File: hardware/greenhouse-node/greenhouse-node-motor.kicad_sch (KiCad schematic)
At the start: 15 parts, among them J7 Conn_01x02_Male, Q2 BC549C, Q3 IRF9530N, Q4 IRF530N, Q6 IRF9530N, Q7 IRF530N, Q8 BC549C

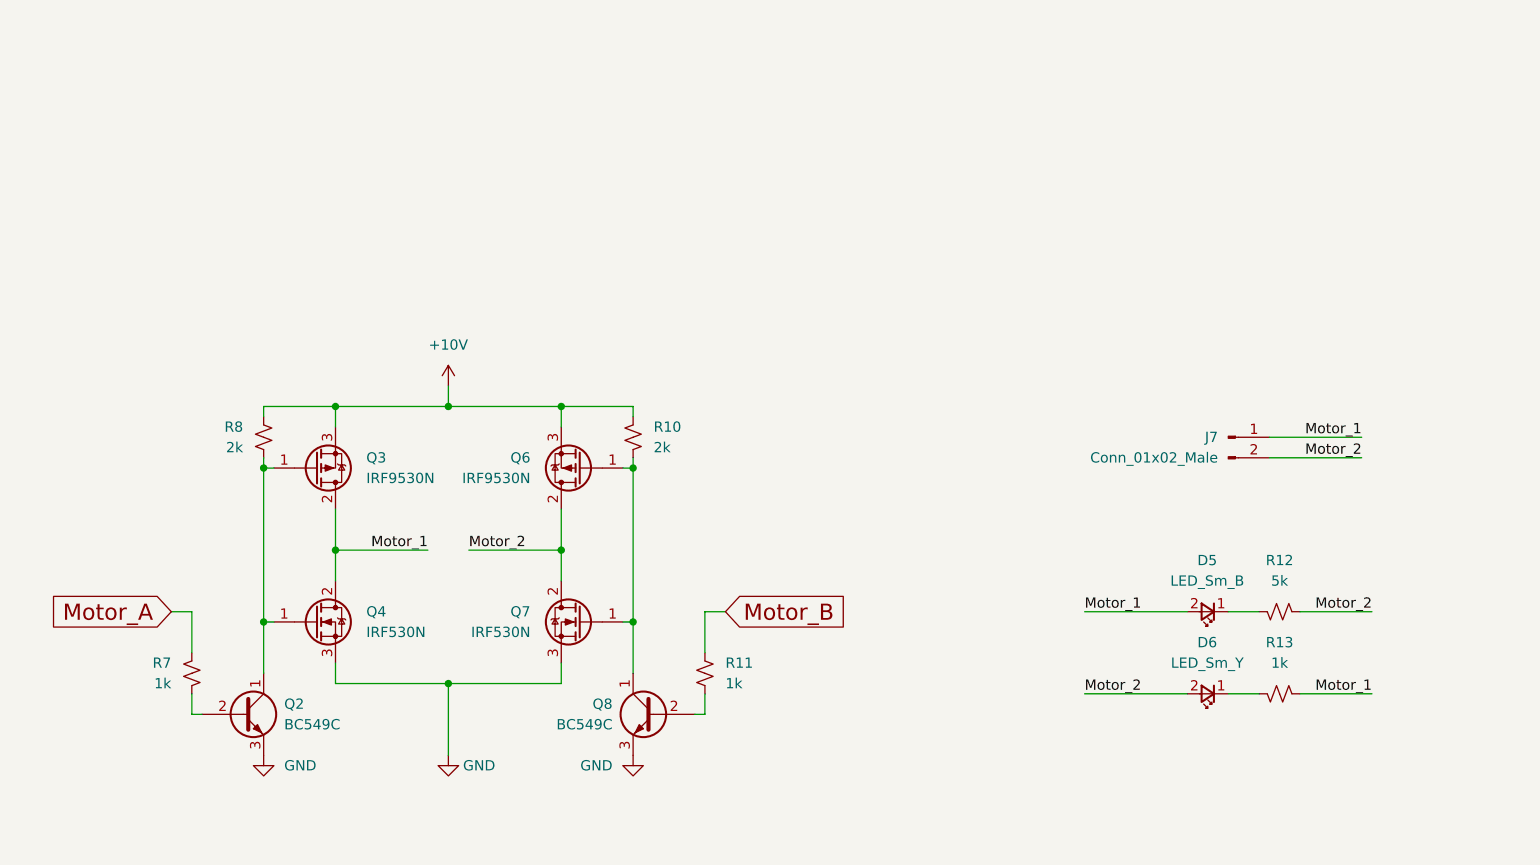
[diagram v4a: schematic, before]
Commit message: Make H-bridge PWM enabled
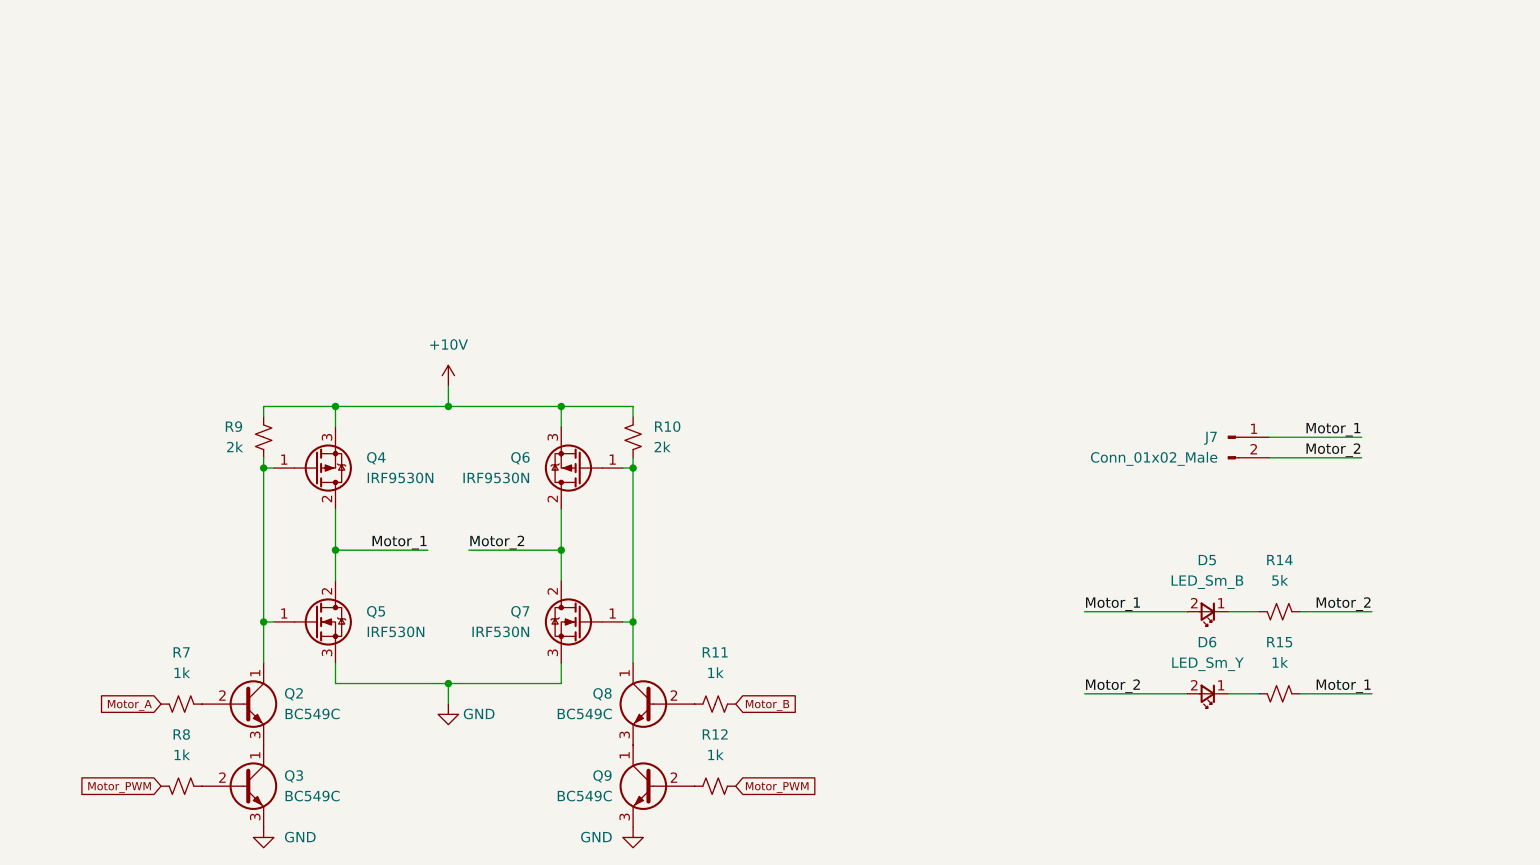
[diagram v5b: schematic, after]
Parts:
- added Q2, Q8: BC549C, Package_TO_SOT_THT:TO-92_Inline, symbol Transistor_BJT:BC549
- added R11, R7: 1k, Resistor_THT:R_Axial_DIN0204_L3.6mm_D1.6mm_P7.62mm_Horizontal, symbol Device:R_Small_US
- renumbered Q2 to Q3, Q3 to Q4, Q4 to Q5, Q8 to Q9, R11 to R12, R12 to R14, R13 to R15, R7 to R8, R8 to R9
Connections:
- net Motor_A: now also R7.2; no longer R8.2
- net Motor_B: now also R11.2; no longer R12.2
- net at Q6.1 (G), Q7.1 (G), R10.1: now also Q8.1 (C); no longer Q9.1 (C)
- net at Q4.1 (G), Q5.1 (G), R9.1: now also Q2.1 (C); no longer Q3.1 (C)
- new net: Q8.3 (E), Q9.1 (C)
- new net: Q2.3 (E), Q3.1 (C)
- new net: Q8.2 (B), R11.1
- new net: Q2.2 (B), R7.1
- new net Motor_PWM: R12.2, R8.2
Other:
- moved on the sheet: Q3, Q9, R12, R8

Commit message: Add pull downs to SR SER+CLK
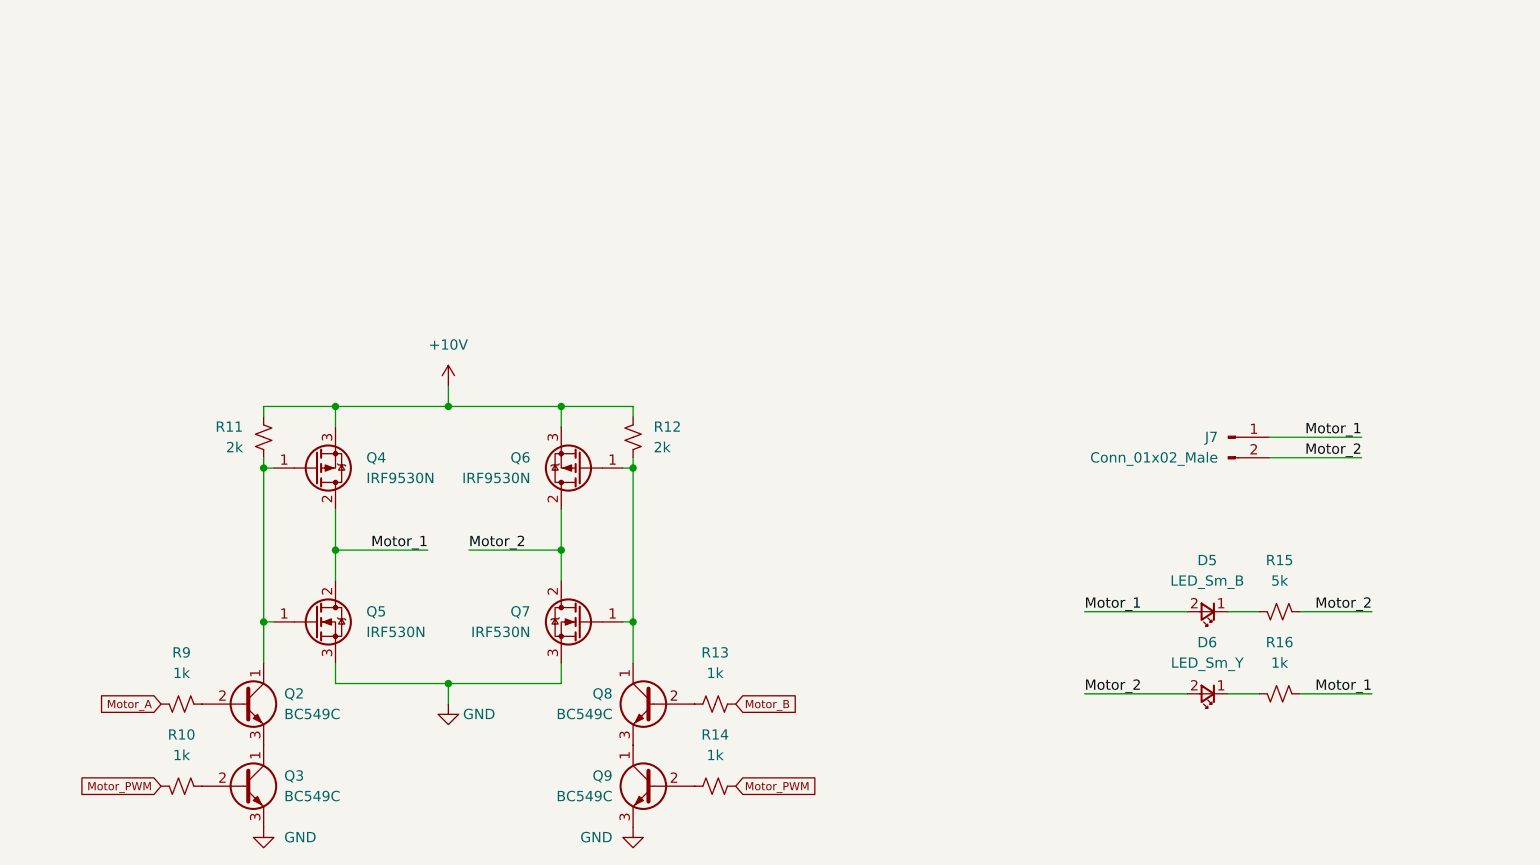
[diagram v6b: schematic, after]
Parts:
- renumbered R8 to R10, R9 to R11, R10 to R12, R11 to R13, R12 to R14, R14 to R15, R15 to R16, R7 to R9
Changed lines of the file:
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@@
   (symbol (lib_id "Device:R_Small_US") (at 69.85 142.24 270) (mirror x) (unit 1)
     (in_bom yes) (on_board yes) (fields_autoplaced)
-    (property "Reference" "R8" (id 0) (at 69.85 135.89 90))
+    (property "Reference" "R10" (id 0) (at 69.85 135.89 90))
     (property "Value" "1k" (id 1) (at 69.85 138.43 90))
     (property "Footprint" "Resistor_THT:R_Axial_DIN0204_L3.6mm_D1.6mm_P7.62mm_Horizontal" (id 2) (at 69.85 142.24 0)
@@
   (symbol (lib_id "power:+10V") (at 102.87 92.71 0) (unit 1)
     (in_bom yes) (on_board yes) (fields_autoplaced)
-    (property "Reference" "#PWR021" (id 0) (at 102.87 96.52 0)
+    (property "Reference" "#PWR022" (id 0) (at 102.87 96.52 0)
       (effects (font (size 1.27 1.27)) hide)
     )
@@
   (symbol (lib_id "Device:R_Small_US") (at 135.89 132.08 90) (unit 1)
     (in_bom yes) (on_board yes) (fields_autoplaced)
-    (property "Reference" "R11" (id 0) (at 135.89 125.73 90))
+    (property "Reference" "R13" (id 0) (at 135.89 125.73 90))
     (property "Value" "1k" (id 1) (at 135.89 128.27 90))
     (property "Footprint" "Resistor_THT:R_Axial_DIN0204_L3.6mm_D1.6mm_P7.62mm_Horizontal" (id 2) (at 135.89 132.08 0)
@@
   (symbol (lib_id "Device:R_Small_US") (at 135.89 142.24 90) (unit 1)
     (in_bom yes) (on_board yes) (fields_autoplaced)
-    (property "Reference" "R12" (id 0) (at 135.89 135.89 90))
+    (property "Reference" "R14" (id 0) (at 135.89 135.89 90))
     (property "Value" "1k" (id 1) (at 135.89 138.43 90))
     (property "Footprint" "Resistor_THT:R_Axial_DIN0204_L3.6mm_D1.6mm_P7.62mm_Horizontal" (id 2) (at 135.89 142.24 0)
@@
   (symbol (lib_id "Device:R_Small_US") (at 69.85 132.08 270) (mirror x) (unit 1)
     (in_bom yes) (on_board yes) (fields_autoplaced)
-    (property "Reference" "R7" (id 0) (at 69.85 125.73 90))
+    (property "Reference" "R9" (id 0) (at 69.85 125.73 90))
     (property "Value" "1k" (id 1) (at 69.85 128.27 90))
     (property "Footprint" "Resistor_THT:R_Axial_DIN0204_L3.6mm_D1.6mm_P7.62mm_Horizontal" (id 2) (at 69.85 132.08 0)
@@
   (symbol (lib_id "Device:R_Small_US") (at 80.01 99.06 180) (unit 1)
     (in_bom yes) (on_board yes) (fields_autoplaced)
-    (property "Reference" "R9" (id 0) (at 77.47 97.7899 0)
+    (property "Reference" "R11" (id 0) (at 77.47 97.7899 0)
       (effects (font (size 1.27 1.27)) (justify left))
     )
@@
   (symbol (lib_id "Device:R_Small_US") (at 125.73 99.06 0) (mirror x) (unit 1)
     (in_bom yes) (on_board yes)
-    (property "Reference" "R10" (id 0) (at 128.27 97.7899 0)
+    (property "Reference" "R12" (id 0) (at 128.27 97.7899 0)
       (effects (font (size 1.27 1.27)) (justify left))
     )
@@
   (symbol (lib_id "Device:R_Small_US") (at 205.74 130.81 270) (mirror x) (unit 1)
     (in_bom yes) (on_board yes) (fields_autoplaced)
-    (property "Reference" "R15" (id 0) (at 205.74 124.46 90))
+    (property "Reference" "R16" (id 0) (at 205.74 124.46 90))
     (property "Value" "1k" (id 1) (at 205.74 127 90))
     (property "Footprint" "Resistor_THT:R_Axial_DIN0204_L3.6mm_D1.6mm_P7.62mm_Horizontal" (id 2) (at 205.74 130.81 0)
@@
   (symbol (lib_id "Device:R_Small_US") (at 205.74 120.65 270) (mirror x) (unit 1)
     (in_bom yes) (on_board yes) (fields_autoplaced)
-    (property "Reference" "R14" (id 0) (at 205.74 114.3 90))
+    (property "Reference" "R15" (id 0) (at 205.74 114.3 90))
     (property "Value" "5k" (id 1) (at 205.74 116.84 90))
     (property "Footprint" "Resistor_THT:R_Axial_DIN0204_L3.6mm_D1.6mm_P7.62mm_Horizontal" (id 2) (at 205.74 120.65 0)
@@
   (symbol (lib_id "power:GND") (at 102.87 132.08 0) (unit 1)
     (in_bom yes) (on_board yes)
-    (property "Reference" "#PWR022" (id 0) (at 102.87 138.43 0)
+    (property "Reference" "#PWR023" (id 0) (at 102.87 138.43 0)
       (effects (font (size 1.27 1.27)) hide)
     )
@@
   (symbol (lib_id "power:GND") (at 80.01 147.32 0) (unit 1)
     (in_bom yes) (on_board yes) (fields_autoplaced)
-    (property "Reference" "#PWR020" (id 0) (at 80.01 153.67 0)
+    (property "Reference" "#PWR021" (id 0) (at 80.01 153.67 0)
       (effects (font (size 1.27 1.27)) hide)
     )
@@
   (symbol (lib_id "power:GND") (at 125.73 147.32 0) (mirror y) (unit 1)
     (in_bom yes) (on_board yes) (fields_autoplaced)
-    (property "Reference" "#PWR023" (id 0) (at 125.73 153.67 0)
-      (effects (font (size 1.27 1.27)) hide)
-    )
+    (property "Reference" "#PWR024" (id 0) (at 125.73 153.67 0)
+      (effects (font (size 1.27 1.27)) hide)
+    )

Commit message: Micro programming connector
Also:
- Connect SRCLR to +5V
- Move 10V pull-up away from micro
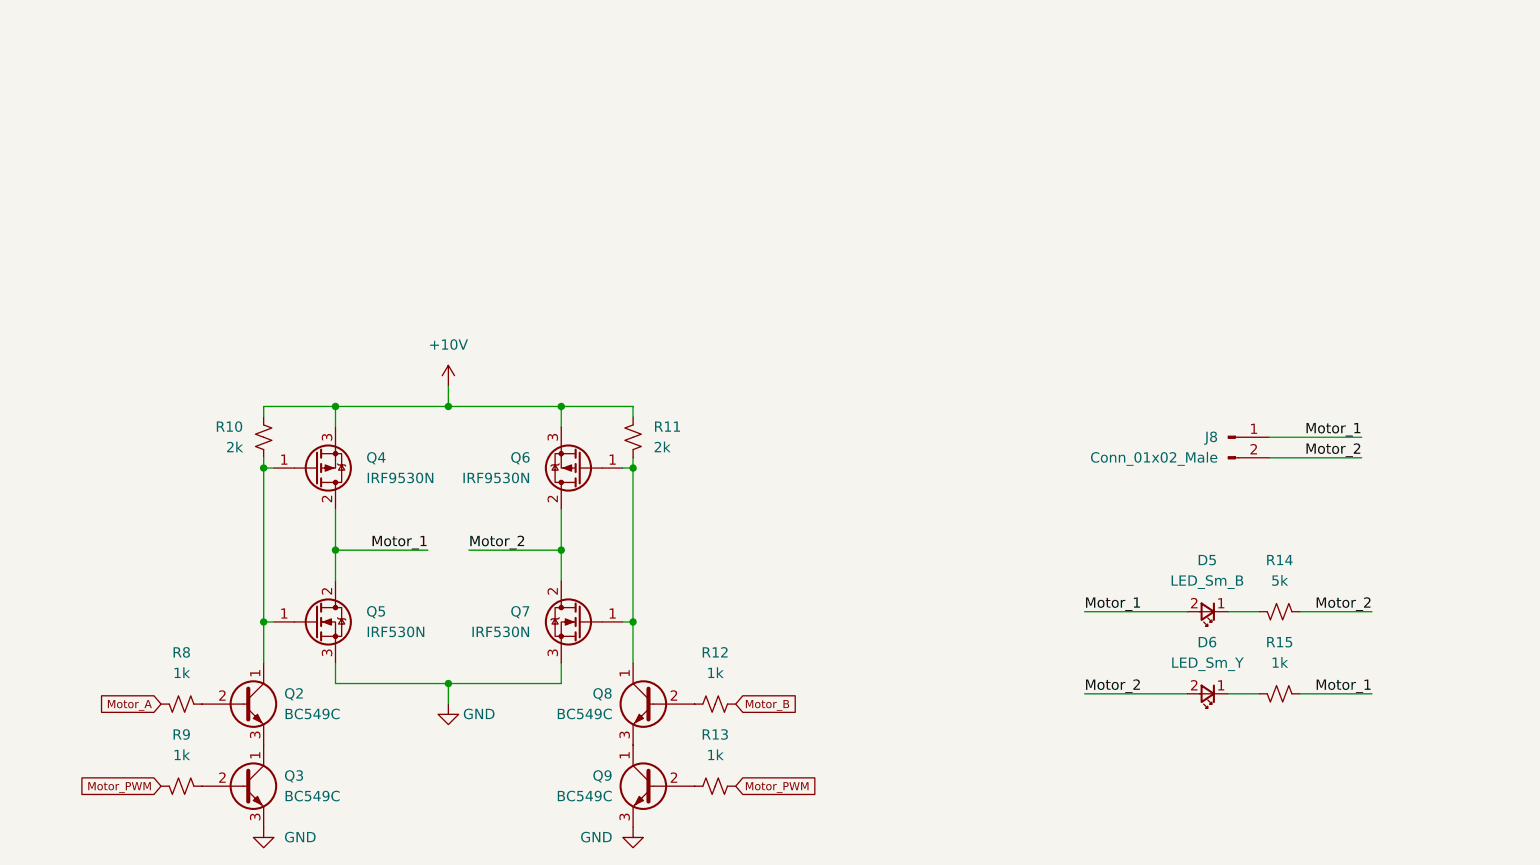
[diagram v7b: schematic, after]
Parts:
- renumbered J7 to J8, R11 to R10, R12 to R11, R13 to R12, R14 to R13, R15 to R14, R16 to R15, R9 to R8, R10 to R9
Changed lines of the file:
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@@
   (symbol (lib_id "Device:R_Small_US") (at 69.85 142.24 270) (mirror x) (unit 1)
     (in_bom yes) (on_board yes) (fields_autoplaced)
-    (property "Reference" "R10" (id 0) (at 69.85 135.89 90))
+    (property "Reference" "R9" (id 0) (at 69.85 135.89 90))
     (property "Value" "1k" (id 1) (at 69.85 138.43 90))
     (property "Footprint" "Resistor_THT:R_Axial_DIN0204_L3.6mm_D1.6mm_P7.62mm_Horizontal" (id 2) (at 69.85 142.24 0)
@@
   (symbol (lib_id "power:+10V") (at 102.87 92.71 0) (unit 1)
     (in_bom yes) (on_board yes) (fields_autoplaced)
-    (property "Reference" "#PWR022" (id 0) (at 102.87 96.52 0)
+    (property "Reference" "#PWR023" (id 0) (at 102.87 96.52 0)
       (effects (font (size 1.27 1.27)) hide)
     )
@@
   (symbol (lib_id "Device:R_Small_US") (at 135.89 132.08 90) (unit 1)
     (in_bom yes) (on_board yes) (fields_autoplaced)
-    (property "Reference" "R13" (id 0) (at 135.89 125.73 90))
+    (property "Reference" "R12" (id 0) (at 135.89 125.73 90))
     (property "Value" "1k" (id 1) (at 135.89 128.27 90))
     (property "Footprint" "Resistor_THT:R_Axial_DIN0204_L3.6mm_D1.6mm_P7.62mm_Horizontal" (id 2) (at 135.89 132.08 0)
@@
   (symbol (lib_id "Connector:Conn_01x02_Male") (at 199.39 99.06 0) (unit 1)
     (in_bom yes) (on_board yes) (fields_autoplaced)
-    (property "Reference" "J7" (id 0) (at 198.12 99.0599 0)
+    (property "Reference" "J8" (id 0) (at 198.12 99.0599 0)
       (effects (font (size 1.27 1.27)) (justify right))
     )
@@
   (symbol (lib_id "Device:R_Small_US") (at 135.89 142.24 90) (unit 1)
     (in_bom yes) (on_board yes) (fields_autoplaced)
-    (property "Reference" "R14" (id 0) (at 135.89 135.89 90))
+    (property "Reference" "R13" (id 0) (at 135.89 135.89 90))
     (property "Value" "1k" (id 1) (at 135.89 138.43 90))
     (property "Footprint" "Resistor_THT:R_Axial_DIN0204_L3.6mm_D1.6mm_P7.62mm_Horizontal" (id 2) (at 135.89 142.24 0)
@@
   (symbol (lib_id "Device:R_Small_US") (at 69.85 132.08 270) (mirror x) (unit 1)
     (in_bom yes) (on_board yes) (fields_autoplaced)
-    (property "Reference" "R9" (id 0) (at 69.85 125.73 90))
+    (property "Reference" "R8" (id 0) (at 69.85 125.73 90))
     (property "Value" "1k" (id 1) (at 69.85 128.27 90))
     (property "Footprint" "Resistor_THT:R_Axial_DIN0204_L3.6mm_D1.6mm_P7.62mm_Horizontal" (id 2) (at 69.85 132.08 0)
@@
   (symbol (lib_id "Device:R_Small_US") (at 80.01 99.06 180) (unit 1)
     (in_bom yes) (on_board yes) (fields_autoplaced)
-    (property "Reference" "R11" (id 0) (at 77.47 97.7899 0)
+    (property "Reference" "R10" (id 0) (at 77.47 97.7899 0)
       (effects (font (size 1.27 1.27)) (justify left))
     )
@@
   (symbol (lib_id "Device:R_Small_US") (at 125.73 99.06 0) (mirror x) (unit 1)
     (in_bom yes) (on_board yes)
-    (property "Reference" "R12" (id 0) (at 128.27 97.7899 0)
+    (property "Reference" "R11" (id 0) (at 128.27 97.7899 0)
       (effects (font (size 1.27 1.27)) (justify left))
     )
@@
   (symbol (lib_id "Device:R_Small_US") (at 205.74 130.81 270) (mirror x) (unit 1)
     (in_bom yes) (on_board yes) (fields_autoplaced)
-    (property "Reference" "R16" (id 0) (at 205.74 124.46 90))
+    (property "Reference" "R15" (id 0) (at 205.74 124.46 90))
     (property "Value" "1k" (id 1) (at 205.74 127 90))
     (property "Footprint" "Resistor_THT:R_Axial_DIN0204_L3.6mm_D1.6mm_P7.62mm_Horizontal" (id 2) (at 205.74 130.81 0)
@@
   (symbol (lib_id "Device:R_Small_US") (at 205.74 120.65 270) (mirror x) (unit 1)
     (in_bom yes) (on_board yes) (fields_autoplaced)
-    (property "Reference" "R15" (id 0) (at 205.74 114.3 90))
+    (property "Reference" "R14" (id 0) (at 205.74 114.3 90))
     (property "Value" "5k" (id 1) (at 205.74 116.84 90))
     (property "Footprint" "Resistor_THT:R_Axial_DIN0204_L3.6mm_D1.6mm_P7.62mm_Horizontal" (id 2) (at 205.74 120.65 0)
@@
   (symbol (lib_id "power:GND") (at 102.87 132.08 0) (unit 1)
     (in_bom yes) (on_board yes)
-    (property "Reference" "#PWR023" (id 0) (at 102.87 138.43 0)
+    (property "Reference" "#PWR024" (id 0) (at 102.87 138.43 0)
       (effects (font (size 1.27 1.27)) hide)
     )
@@
   (symbol (lib_id "power:GND") (at 80.01 147.32 0) (unit 1)
     (in_bom yes) (on_board yes) (fields_autoplaced)
-    (property "Reference" "#PWR021" (id 0) (at 80.01 153.67 0)
+    (property "Reference" "#PWR022" (id 0) (at 80.01 153.67 0)
       (effects (font (size 1.27 1.27)) hide)
     )
@@
   (symbol (lib_id "power:GND") (at 125.73 147.32 0) (mirror y) (unit 1)
     (in_bom yes) (on_board yes) (fields_autoplaced)
-    (property "Reference" "#PWR024" (id 0) (at 125.73 153.67 0)
-      (effects (font (size 1.27 1.27)) hide)
-    )
+    (property "Reference" "#PWR025" (id 0) (at 125.73 153.67 0)
+      (effects (font (size 1.27 1.27)) hide)
+    )
